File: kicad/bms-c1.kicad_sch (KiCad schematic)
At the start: 42 parts, among them J1 MicroFit 2x7, J10 Conn_01x06, J2 UEXT, J3 USB_B_Micro, J4 Conn_01x05, J5 MicroFit 2x9, J6 Conn_01x02, J9 Conn_01x06

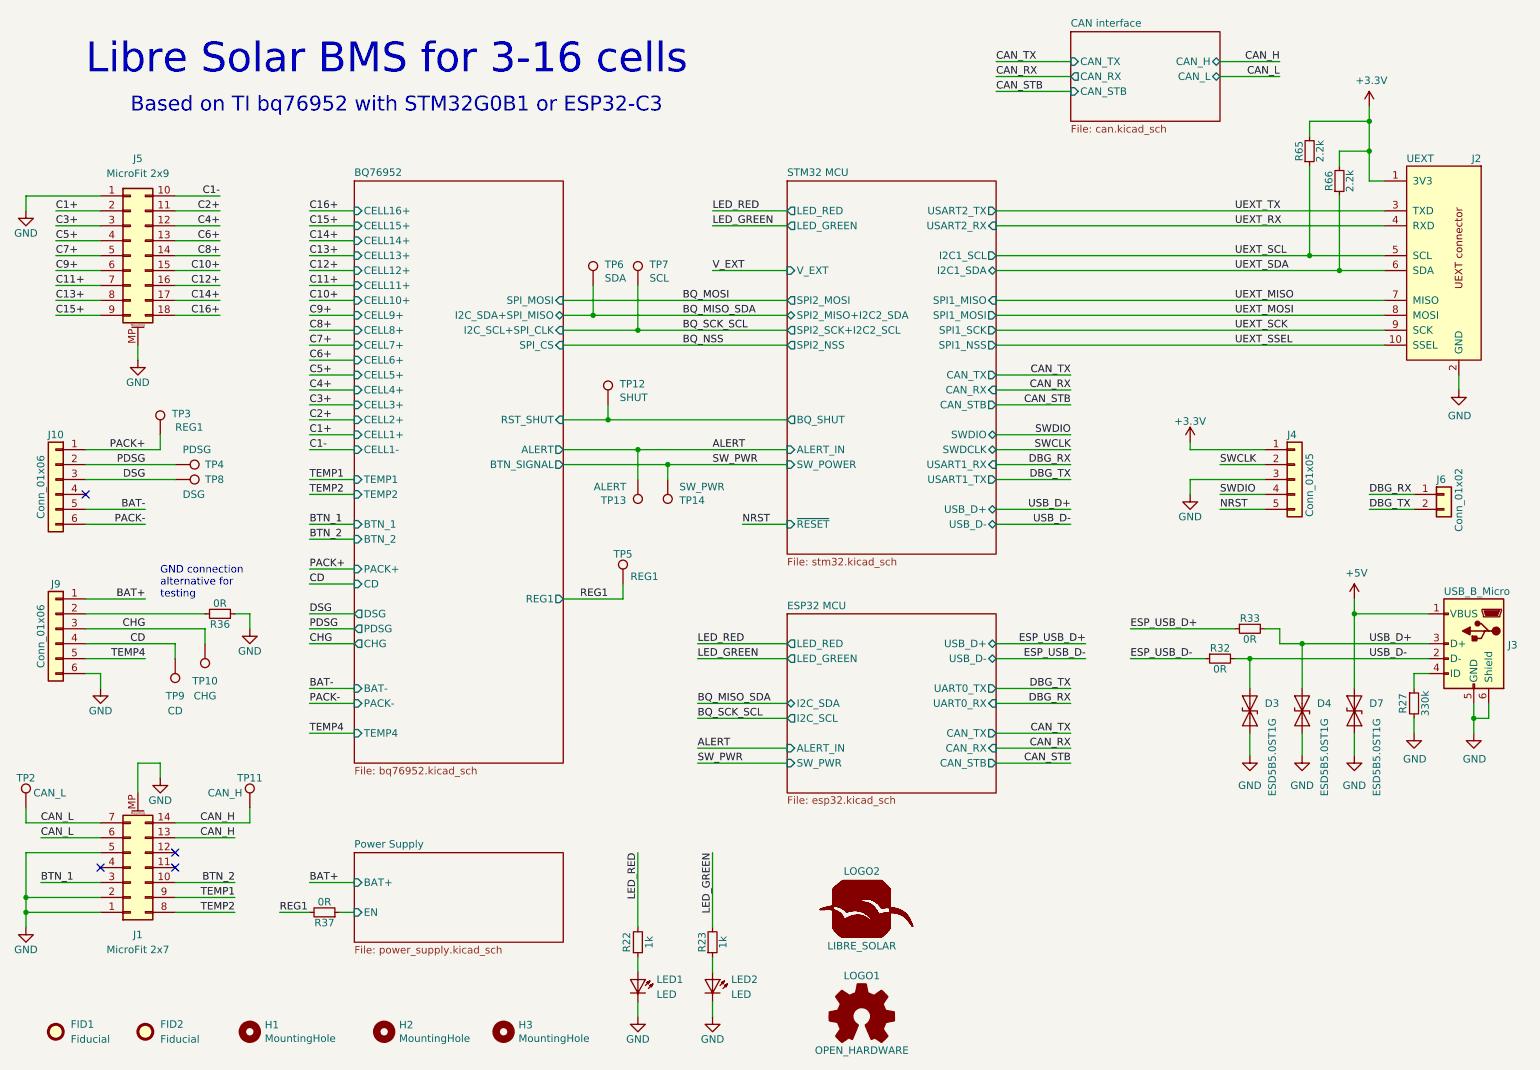
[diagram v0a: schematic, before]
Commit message: Major update for BMS C1 v0.3
This commit contains major updates of the PCB after the first prototype
build-up and testing. Changes include:

- Single PCB instead of stacked PCBs to simplify design and reduce cost.
- STM32 MCU was removed due to supply shortage. Only ESP32-C3 supported.
- Custom connectors replaced with off-the-shelf Würth Power Elements.
- 5V power rail removed to simplify design (CAN runs on 3V3 transceiver).
- Larger Shunt with improved footprint.
- Optimized layout to reduce distance between IC and shunt.
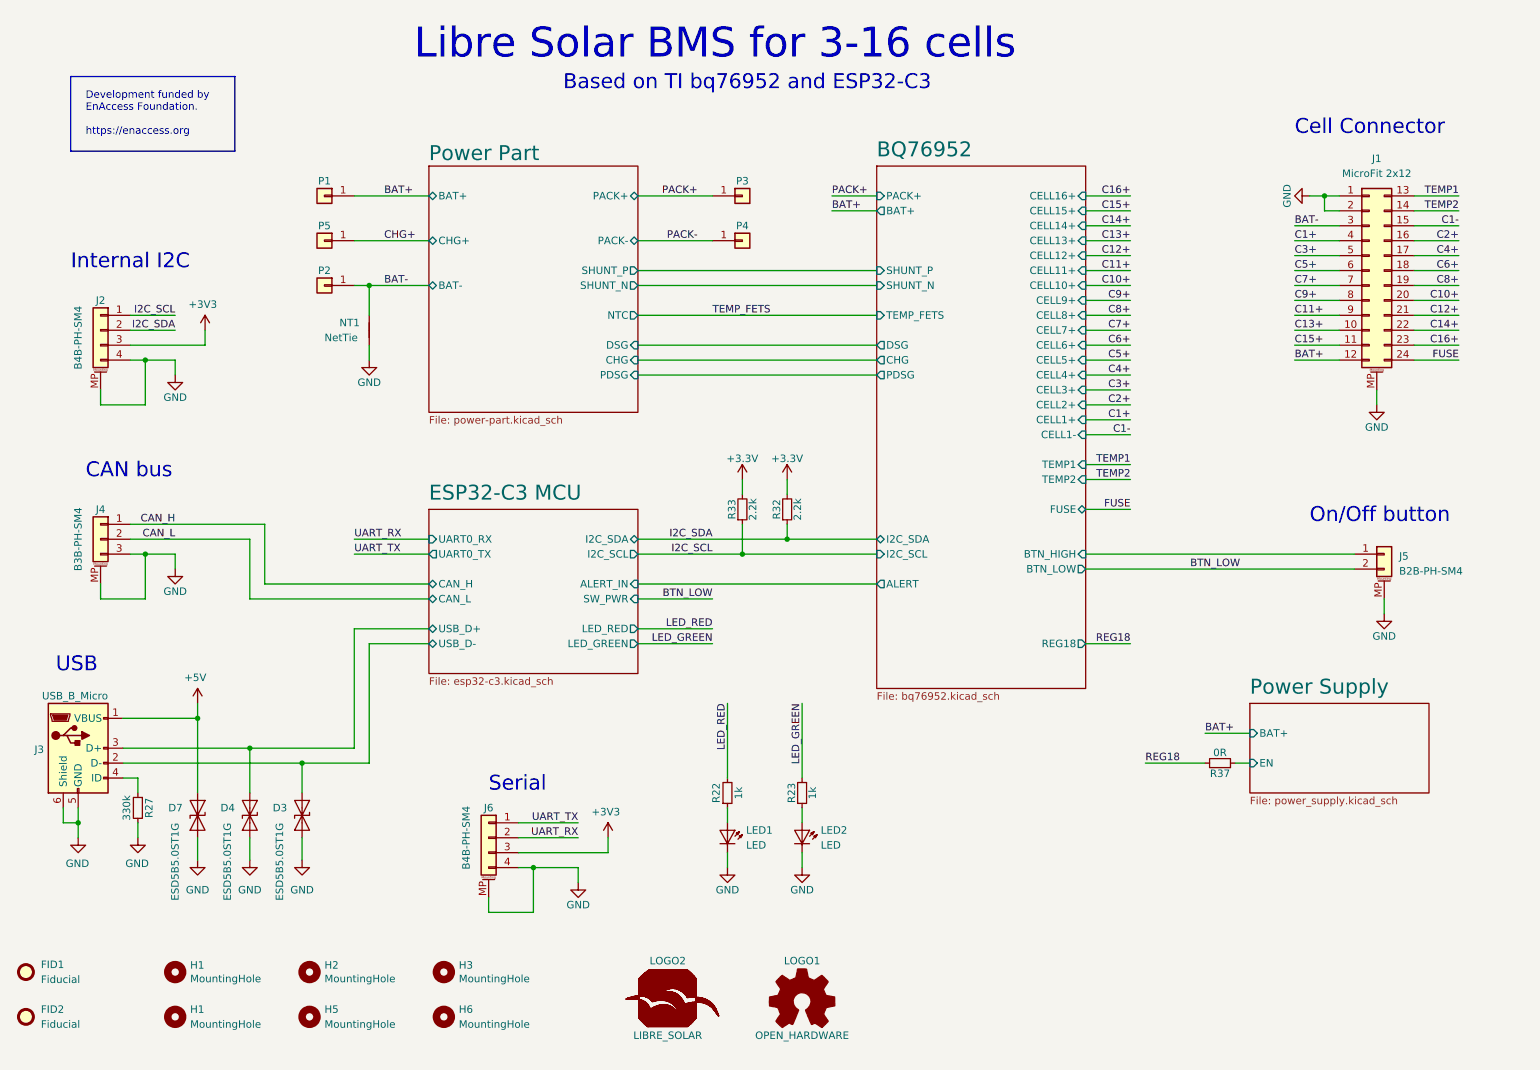
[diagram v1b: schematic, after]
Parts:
- removed J1: MicroFit 2x7, Connector_Molex:Molex_Micro-Fit_3.0_43045-1410_2x07-1MP_P3.00mm_Horizontal, symbol Connector_Generic_MountingPin:Conn_02x07_Top_Bottom_MountingPin
- removed J10, J9: Conn_01x06, Connector_PinSocket_2.00mm:PinSocket_1x06_P2.00mm_Vertical, symbol Connector_Generic:Conn_01x06
- removed J2: UEXT, LibreSolar:Box_Header_2x05x2.54mm_Straight, symbol LibreSolar:UEXT
- removed J4: Conn_01x05, Connector_PinHeader_2.54mm:PinHeader_1x05_P2.54mm_Vertical, symbol Connector_Generic:Conn_01x05
- removed J6: Conn_01x02, Connector_PinHeader_2.54mm:PinHeader_1x02_P2.54mm_Vertical, symbol Connector_Generic:Conn_01x02
- removed R36: 0R, LibreSolar:R_0603_1608, symbol LibreSolar:R
- removed R65, R66: 2.2k, LibreSolar:R_0603_1608, symbol LibreSolar:R
- removed TP10: CHG, TestPoint:TestPoint_Pad_D1.5mm, symbol Connector:TestPoint
- removed TP11: CAN_H, TestPoint:TestPoint_Pad_D1.5mm, symbol Connector:TestPoint
- removed TP12: SHUT, TestPoint:TestPoint_Pad_D1.5mm, symbol Connector:TestPoint
- removed TP13: ALERT, TestPoint:TestPoint_Pad_D1.5mm, symbol Connector:TestPoint
- removed TP14: SW_PWR, TestPoint:TestPoint_Pad_D1.5mm, symbol Connector:TestPoint
- removed TP2: CAN_L, TestPoint:TestPoint_Pad_D1.5mm, symbol Connector:TestPoint
- removed TP3, TP5: REG1, TestPoint:TestPoint_Pad_D1.5mm, symbol Connector:TestPoint
- removed TP4: PDSG, TestPoint:TestPoint_Pad_D1.5mm, symbol Connector:TestPoint
- removed TP6: SDA, TestPoint:TestPoint_Pad_D1.5mm, symbol Connector:TestPoint
- removed TP7: SCL, TestPoint:TestPoint_Pad_D1.5mm, symbol Connector:TestPoint
- removed TP8: DSG, TestPoint:TestPoint_Pad_D1.5mm, symbol Connector:TestPoint
- removed TP9: CD, TestPoint:TestPoint_Pad_D1.5mm, symbol Connector:TestPoint
- added H1, H5, H6: MountingHole, MountingHole:MountingHole_3.2mm_M3_Pad_TopBottom, symbol Mechanical:MountingHole
- added J2, J6: B4B-PH-SM4, Connector_JST:JST_PH_B4B-PH-SM4-TB_1x04-1MP_P2.00mm_Vertical, symbol Connector_Generic_MountingPin:Conn_01x04_MountingPin
- added J4: B3B-PH-SM4, Connector_JST:JST_PH_B3B-PH-SM4-TB_1x03-1MP_P2.00mm_Vertical, symbol Connector_Generic_MountingPin:Conn_01x03_MountingPin
- added J5: B2B-PH-SM4, Connector_JST:JST_PH_B2B-PH-SM4-TB_1x02-1MP_P2.00mm_Vertical, symbol Connector_Generic_MountingPin:Conn_01x02_MountingPin
- added NT1: NetTie_2, NetTie:NetTie-2_SMD_Pad0.5mm, symbol Device:NetTie_2
- added P1, P2, P3, P4: CONN_01X01, LibreSolar:Wuerth_WP-BUCF_7460408_Plated, symbol Connector_Generic:Conn_01x01
- added P5: CONN_01X01, Connector_Wire:SolderWirePad_1x01_SMD_5x10mm, symbol Connector_Generic:Conn_01x01
- D3, D4, D7: footprint Diode_SMD:D_SOD-523 -> LibreSolar:D_SOD-523
- H1, H2, H3: footprint MountingHole:MountingHole_3.2mm_M3 -> MountingHole:MountingHole_3.2mm_M3_Pad_TopBottom
- J1: renamed from J5; value MicroFit 2x9 -> MicroFit 2x12; footprint Connector_Molex:Molex_Micro-Fit_3.0_43045-1810_2x09-1MP_P3.00mm_Horizontal -> Connector_Molex:Molex_Micro-Fit_3.0_43045-2410_2x12-1MP_P3.00mm_Horizontal; symbol Connector_Generic_MountingPin:Conn_02x09_Top_Bottom_MountingPin -> Connector_Generic_MountingPin:Conn_02x12_Top_Bottom_MountingPin
- R32, R33: value 0R -> 2.2k
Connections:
- net +3V3: now also R32.2, R33.2, J2.3 (Pin_3), J6.3 (Pin_3)
- net BAT+: now also J1.12 (Pin_12), P1.1 (Pin_1)
- net BAT-: now also J1.3 (Pin_3), NT1.1, P2.1 (Pin_1)
- net C1+: now also J1.4 (Pin_4); no longer J1.2 (Pin_2)
- net C1-: now also J1.15 (Pin_15); no longer J1.10 (Pin_10)
- net C10+: now also J1.20 (Pin_20); no longer J1.15 (Pin_15)
- net C11+: now also J1.9 (Pin_9); no longer J1.7 (Pin_7)
- net C12+: now also J1.21 (Pin_21); no longer J1.16 (Pin_16)
- net C13+: now also J1.10 (Pin_10); no longer J1.8 (Pin_8)
- net C14+: now also J1.22 (Pin_22); no longer J1.17 (Pin_17)
- net C15+: now also J1.11 (Pin_11); no longer J1.9 (Pin_9)
- net C16+: now also J1.23 (Pin_23); no longer J1.18 (Pin_18)
- net C2+: now also J1.16 (Pin_16); no longer J1.11 (Pin_11)
- net C3+: now also J1.5 (Pin_5); no longer J1.3 (Pin_3)
- net C4+: now also J1.17 (Pin_17); no longer J1.12 (Pin_12)
- net C5+: now also J1.6 (Pin_6); no longer J1.4 (Pin_4)
- net C6+: now also J1.18 (Pin_18); no longer J1.13 (Pin_13)
- net C7+: now also J1.7 (Pin_7); no longer J1.5 (Pin_5)
- net C8+: now also J1.19 (Pin_19); no longer J1.14 (Pin_14)
- net C9+: now also J1.8 (Pin_8); no longer J1.6 (Pin_6)
- net CAN_H: now also J4.1 (Pin_1)
- net CAN_L: now also J4.2 (Pin_2)
- net GND: now also J1.2 (Pin_2), J2.4 (Pin_4), J2.MP (MountPin), J4.3 (Pin_3), J4.MP (MountPin), J5.MP (MountPin), J6.4 (Pin_4), J6.MP (MountPin), NT1.2
- net PACK+: now also P3.1 (Pin_1)
- net PACK-: now also P4.1 (Pin_1)
- net TEMP1: now also J1.13 (Pin_13)
- net TEMP2: now also J1.14 (Pin_14)
- net ESP_USB_D+ renamed I2C_SCL
- net I2C_SCL: now also J2.1 (Pin_1)
- net ESP_USB_D- renamed I2C_SDA
- net I2C_SDA: now also J2.2 (Pin_2)
- net REG1 renamed REG18
- net USB_D+ renamed ESP32-C3 MCU/USB_D+
- net ESP32-C3 MCU/USB_D+: no longer R33.2
- net USB_D- renamed ESP32-C3 MCU/USB_D-
- net ESP32-C3 MCU/USB_D-: no longer R32.2
- new net BQ76952/BTN_HIGH: J5.1 (Pin_1)
- new net BTN_LOW: J5.2 (Pin_2)
- new net CHG+: P5.1 (Pin_1)
- new net FUSE: J1.24 (Pin_24)
- new net UART_RX: J6.2 (Pin_2)
- new net UART_TX: J6.1 (Pin_1)
- no-connect marks 4 -> 0
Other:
- removed sheet CAN interface
- removed sheet ESP32 MCU
- removed sheet STM32 MCU
- added sheet ESP32-C3 MCU (esp32-c3.kicad_sch)
- added sheet Power Part (power-part.kicad_sch)
- sheet BQ76952 ports: added BAT+, BTN_HIGH, BTN_LOW, FUSE, I2C_SCL, I2C_SDA, REG18, SHUNT_N, SHUNT_P, TEMP_FETS; removed BAT-, BTN_1, BTN_2, BTN_SIGNAL, CD, I2C_SCL+SPI_CLK, I2C_SDA+SPI_MISO, PACK-, REG1, RST_SHUT, SPI_CS, SPI_MOSI, TEMP4
- note added: "Based on TI bq76952 and ESP32-C3"
- note added: "CAN bus"
- note added: "Cell Connector"
- note added: "Development funded by EnAccess Foundation. https://enaccess.org"
- note added: "Internal I2C"
- note added: "On/Off button"
- note added: "Serial"
- note added: "USB"
- note removed: "Based on TI bq76952 with STM32G0B1 or ESP32-C3"
- note removed: "GND connection alternative for testing"
- title: BMS 16S Control Board -> Libre Solar BMS C1
- moved on the sheet: D3, D4, D7, FID1, FID2, H1, H2, H3, J3, LED1, LED2, LOGO1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

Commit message: BOM updates with a few more alternative parts
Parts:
- D3, D4, D7: Manufacturer (none) -> onsemi; PartNumber (none) -> ESD5B5.0ST1G
- J1: Remarks Alternative: Würth 662018231722, 662118231722, mating conne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 -> Alternative: Würth 662024231722, mating connector: 66202411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
- J2, J6: Manufacturer (none) -> JST; Remarks (none) -> Alternative: Würth 620304124022
- J4: Manufacturer (none) -> JST; Remarks (none) -> Alternative: Würth 620303124022
- J5: Remarks (none) -> Alternative: Würth 620302124022
- P1, P2, P3, P4: PartNumber (none) -> 7460408
- P5: Manufacturer Würth -> (none)
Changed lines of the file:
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@@
+      (effects (font (size 1.27 1.27)) hide)
+    )
+    (property "Manufacturer" "JST" (id 4) (at 35.56 71.12 0)
+      (effects (font (size 1.27 1.27)) hide)
+    )
+    (property "Remarks" "Alternative: Würth 620304124022" (id 5) (at 35.56 71.12 0)
       (effects (font (size 1.27 1.27)) hide)
     )
@@
       (effects (font (size 1.27 1.27)) hide)
     )
+    (property "Remarks" "Alternative: Würth 620302124022" (id 8) (at 254 109.22 0)
+      (effects (font (size 1.27 1.27)) hide)
+    )
     (pin "1")
     (pin "2")
@@
     )
     (property "Datasheet" "https://www.mouser.de/datasheet/2/308/1/ESD5B5_0ST1_D-2311335.pdf" (id 3) (at 69.85 153.67 0)
+      (effects (font (size 1.27 1.27)) hide)
+    )
+    (property "Manufacturer" "onsemi" (id 4) (at 69.85 153.67 0)
+      (effects (font (size 1.27 1.27)) hide)
+    )
+    (property "PartNumber" "ESD5B5.0ST1G" (id 5) (at 69.85 153.67 0)
       (effects (font (size 1.27 1.27)) hide)
     )
@@
       (effects (font (size 1.27 1.27)) hide)
     )
-    (property "Remarks" "Alternative: Würth 662018231722, 662118231722, mating connector: 662018113322" (id 6) (at 251.46 60.96 0)
+    (property "Remarks" "Alternative: Würth 662024231722, mating connector: 662024113322" (id 6) (at 251.46 60.96 0)
       (effects (font (size 1.27 1.27)) hide)
     )
@@
       (effects (font (size 1.27 1.27)) hide)
     )
+    (property "PartNumber" "7460408" (id 5) (at 144.78 55.88 0)
+      (effects (font (size 1.27 1.27)) hide)
+    )
     (pin "1")
   )
@@
       (effects (font (size 1.524 1.524)) hide)
     )
+    (property "PartNumber" "7460408" (id 5) (at 73.66 63.5 0)
+      (effects (font (size 1.27 1.27)) hide)
+    )
     (pin "1")
   )
@@
       (effects (font (size 1.524 1.524)) hide)
     )
+    (property "PartNumber" "7460408" (id 5) (at 144.78 48.26 0)
+      (effects (font (size 1.27 1.27)) hide)
+    )
     (pin "1")
   )
@@
     )
     (property "Datasheet" "" (id 3) (at 73.66 55.88 0))
-    (property "Manufacturer" "Würth" (id 4) (at 73.66 55.88 0)
+    (property "Manufacturer" "" (id 4) (at 73.66 55.88 0)
       (effects (font (size 1.524 1.524)) hide)
     )
@@
       (effects (font (size 1.27 1.27)) hide)
     )
+    (property "Manufacturer" "JST" (id 7) (at 35.56 106.68 0)
+      (effects (font (size 1.27 1.27)) hide)
+    )
+    (property "Remarks" "Alternative: Würth 620303124022" (id 8) (at 35.56 106.68 0)
+      (effects (font (size 1.27 1.27)) hide)
+    )
     (pin "1")
     (pin "2")
@@
     )
     (property "Datasheet" "https://www.mouser.de/datasheet/2/308/1/ESD5B5_0ST1_D-2311335.pdf" (id 3) (at 52.07 153.67 0)
+      (effects (font (size 1.27 1.27)) hide)
+    )
+    (property "Manufacturer" "onsemi" (id 4) (at 52.07 153.67 0)
+      (effects (font (size 1.27 1.27)) hide)
+    )
+    (property "PartNumber" "ESD5B5.0ST1G" (id 5) (at 52.07 153.67 0)
       (effects (font (size 1.27 1.27)) hide)
     )
@@
       (effects (font (size 1.27 1.27)) hide)
     )
+    (property "Manufacturer" "onsemi" (id 4) (at 60.96 153.67 0)
+      (effects (font (size 1.27 1.27)) hide)
+    )
+    (property "PartNumber" "ESD5B5.0ST1G" (id 5) (at 60.96 153.67 0)
+      (effects (font (size 1.27 1.27)) hide)
+    )
     (pin "1")
     (pin "2")
@@
       (effects (font (size 1.27 1.27)) hide)
     )
+    (property "Manufacturer" "JST" (id 7) (at 101.6 157.48 0)
+      (effects (font (size 1.27 1.27)) hide)
+    )
+    (property "Remarks" "Alternative: Würth 620304124022" (id 8) (at 101.6 157.48 0)
+      (effects (font (size 1.27 1.27)) hide)
+    )
     (pin "1")
     (pin "2")
@@
       (effects (font (size 1.524 1.524)) hide)
     )
-    (pin "1")
+    (property "PartNumber" "7460408" (id 5) (at 73.66 48.26 0)
+      (effects (font (size 1.27 1.27)) hide)
+    )
+    (pin "1")

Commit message: v3.2.2: Switch to SMD terminals instead of press-fit
Rationale: These are easier to manufacture (no additional step required)
and the PCB can be mounted onto a heat sink without any milling required.
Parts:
- P1, P2, P3, P4: footprint LibreSolar:Wuerth_WP-BUCF_7460408_Plated -> LibreSolar:Wuerth_PowerOne_SMD_LF990005; PartNumber 7460408 -> LF990005; Remarks (none) -> Alternative: Erni 225852
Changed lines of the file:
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@@
   (title_block
     (title "Libre Solar BMS C1")
-    (date "2022-09-30")
-    (rev "0.3.1")
+    (date "2022-11-07")
+    (rev "0.3.2")
     (company "Libre Solar Technologies GmbH")
     (comment 1 "Website: https://libre.solar")
@@
       (effects (font (size 1.27 1.27)) hide)
     )
-    (property "Footprint" "LibreSolar:Wuerth_WP-BUCF_7460408_Plated" (id 2) (at 144.78 55.88 0)
+    (property "Footprint" "LibreSolar:Wuerth_PowerOne_SMD_LF990005" (id 2) (at 144.78 55.88 0)
       (effects (font (size 1.27 1.27)) hide)
     )
@@
       (effects (font (size 1.27 1.27)) hide)
     )
-    (property "PartNumber" "7460408" (id 5) (at 144.78 55.88 0)
+    (property "PartNumber" "LF990005" (id 5) (at 144.78 55.88 0)
+      (effects (font (size 1.27 1.27)) hide)
+    )
+    (property "Remarks" "Alternative: Erni 225852" (id 6) (at 144.78 55.88 0)
       (effects (font (size 1.27 1.27)) hide)
     )
@@
       (effects (font (size 1.27 1.27)) hide)
     )
-    (property "Footprint" "LibreSolar:Wuerth_WP-BUCF_7460408_Plated" (id 2) (at 73.66 63.5 0)
+    (property "Footprint" "LibreSolar:Wuerth_PowerOne_SMD_LF990005" (id 2) (at 73.66 63.5 0)
       (effects (font (size 1.27 1.27)) hide)
     )
@@
       (effects (font (size 1.524 1.524)) hide)
     )
-    (property "PartNumber" "7460408" (id 5) (at 73.66 63.5 0)
+    (property "PartNumber" "LF990005" (id 5) (at 73.66 63.5 0)
+      (effects (font (size 1.27 1.27)) hide)
+    )
+    (property "Remarks" "Alternative: Erni 225852" (id 6) (at 73.66 63.5 0)
       (effects (font (size 1.27 1.27)) hide)
     )
@@
       (effects (font (size 1.27 1.27)) hide)
     )
-    (property "Footprint" "LibreSolar:Wuerth_WP-BUCF_7460408_Plated" (id 2) (at 144.78 48.26 0)
+    (property "Footprint" "LibreSolar:Wuerth_PowerOne_SMD_LF990005" (id 2) (at 144.78 48.26 0)
       (effects (font (size 1.27 1.27)) hide)
     )
@@
       (effects (font (size 1.524 1.524)) hide)
     )
-    (property "PartNumber" "7460408" (id 5) (at 144.78 48.26 0)
+    (property "PartNumber" "LF990005" (id 5) (at 144.78 48.26 0)
+      (effects (font (size 1.27 1.27)) hide)
+    )
+    (property "Remarks" "Alternative: Erni 225852" (id 6) (at 144.78 48.26 0)
       (effects (font (size 1.27 1.27)) hide)
     )
@@
       (effects (font (size 1.27 1.27)) hide)
     )
-    (property "Footprint" "LibreSolar:Wuerth_WP-BUCF_7460408_Plated" (id 2) (at 73.66 48.26 0)
+    (property "Footprint" "LibreSolar:Wuerth_PowerOne_SMD_LF990005" (id 2) (at 73.66 48.26 0)
       (effects (font (size 1.27 1.27)) hide)
     )
@@
       (effects (font (size 1.524 1.524)) hide)
     )
-    (property "PartNumber" "7460408" (id 5) (at 73.66 48.26 0)
+    (property "PartNumber" "LF990005" (id 5) (at 73.66 48.26 0)
+      (effects (font (size 1.27 1.27)) hide)
+    )
+    (property "Remarks" "Alternative: Erni 225852" (id 6) (at 73.66 48.26 0)
       (effects (font (size 1.27 1.27)) hide)
     )
@@
     )
     (path "/fdaa24bf-886a-4fae-9272-9a620f068ae0"
-      (reference "P1") (unit 1) (value "CONN_01X01") (footprint "LibreSolar:Wuerth_WP-BUCF_7460408_Plated")
+      (reference "P1") (unit 1) (value "CONN_01X01") (footprint "LibreSolar:Wuerth_PowerOne_SMD_LF990005")
     )
     (path "/29a612a2-5824-4116-80be-b8df3e29c6a4"
-      (reference "P2") (unit 1) (value "CONN_01X01") (footprint "LibreSolar:Wuerth_WP-BUCF_7460408_Plated")
+      (reference "P2") (unit 1) (value "CONN_01X01") (footprint "LibreSolar:Wuerth_PowerOne_SMD_LF990005")
     )
     (path "/2d9c6ce9-8271-4860-bf0e-b73836f0c1f3"
-      (reference "P3") (unit 1) (value "CONN_01X01") (footprint "LibreSolar:Wuerth_WP-BUCF_7460408_Plated")
+      (reference "P3") (unit 1) (value "CONN_01X01") (footprint "LibreSolar:Wuerth_PowerOne_SMD_LF990005")
     )
     (path "/1aadcf9d-31bf-4fc7-b6f1-8354b5a5a35d"
-      (reference "P4") (unit 1) (value "CONN_01X01") (footprint "LibreSolar:Wuerth_WP-BUCF_7460408_Plated")
+      (reference "P4") (unit 1) (value "CONN_01X01") (footprint "LibreSolar:Wuerth_PowerOne_SMD_LF990005")
     )
     (path "/3f65028a-515e-4f29-99b7-3e7899216a5d"
